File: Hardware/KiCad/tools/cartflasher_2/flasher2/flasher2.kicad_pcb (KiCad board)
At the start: 4 copper layers, 89 x 93 mm, 31 parts, among them J1 USB_C_Receptacle_USB2.0, J2 ICSP, SW1 SW_Push, U2 AVR64DA64-I/PT, U3 FT232RL

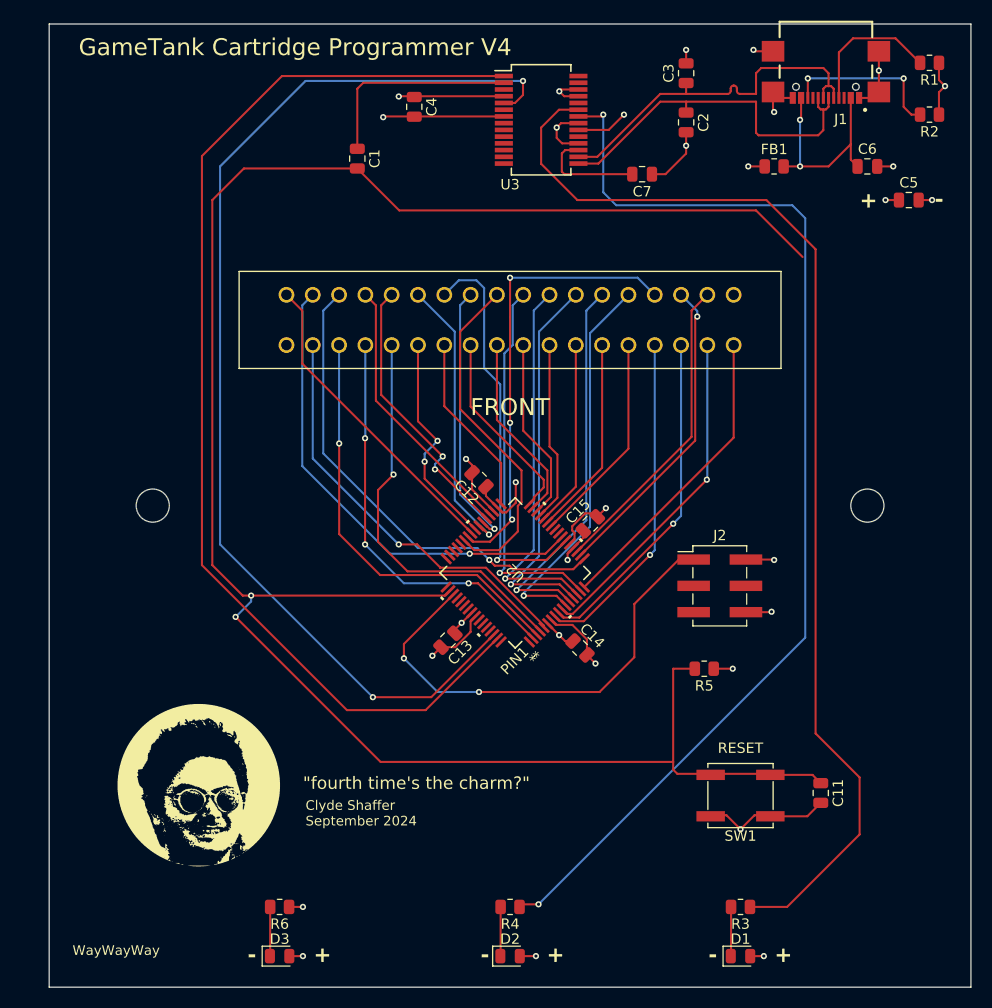
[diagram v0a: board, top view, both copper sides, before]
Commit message: flasher2 sent for prototype production
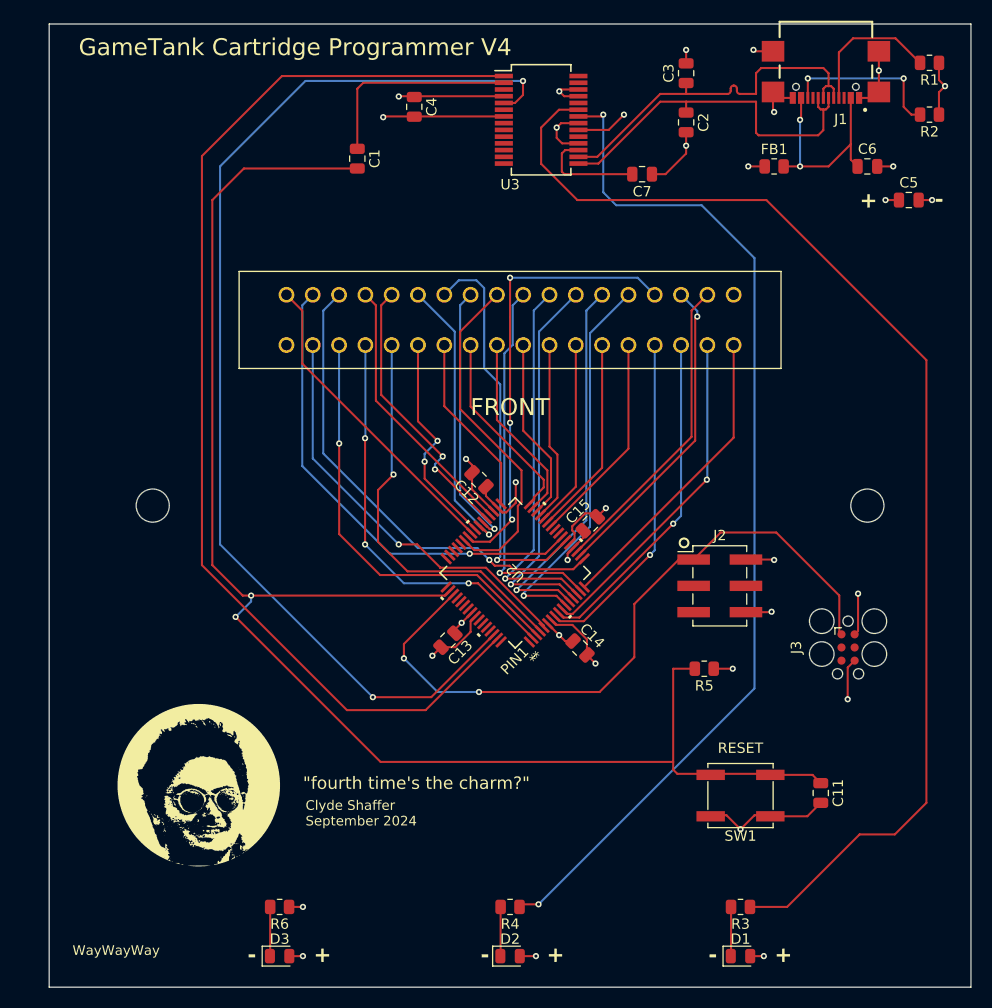
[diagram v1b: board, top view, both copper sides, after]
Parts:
- added J3: ICSP, Connector:Tag-Connect_TC2030-IDC-FP_2x03_P1.27mm_Vertical, F.Cu at (177.1, 120.2)
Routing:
- net /~{mcuRESET}: track 198.7 -> 152.2 mm
- net /UPDI: track 45.8 -> 67.3 mm
- net /rxl: track 109.4 -> 100.2 mm
- net /txl: track 109.5 -> 116.8 mm
- net VCC: track 42.9 -> 47.0 mm, vias 13 -> 14
- net GND: track 91.0 -> 95.0 mm, vias 18 -> 19
